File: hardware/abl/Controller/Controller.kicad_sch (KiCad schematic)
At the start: 21 parts, among them IC1 LSF0204PWJ, IC3 VEML6040A3OG, IC4 FXL6408UMX, J1 SFW20S-2STE1LF, J2 Conn_02x03_Odd_Even, J3 Conn_02x03_Odd_Even, J4 PRT-14417, J5 Conn_02x04_Odd_Even, U1 INA219AxD

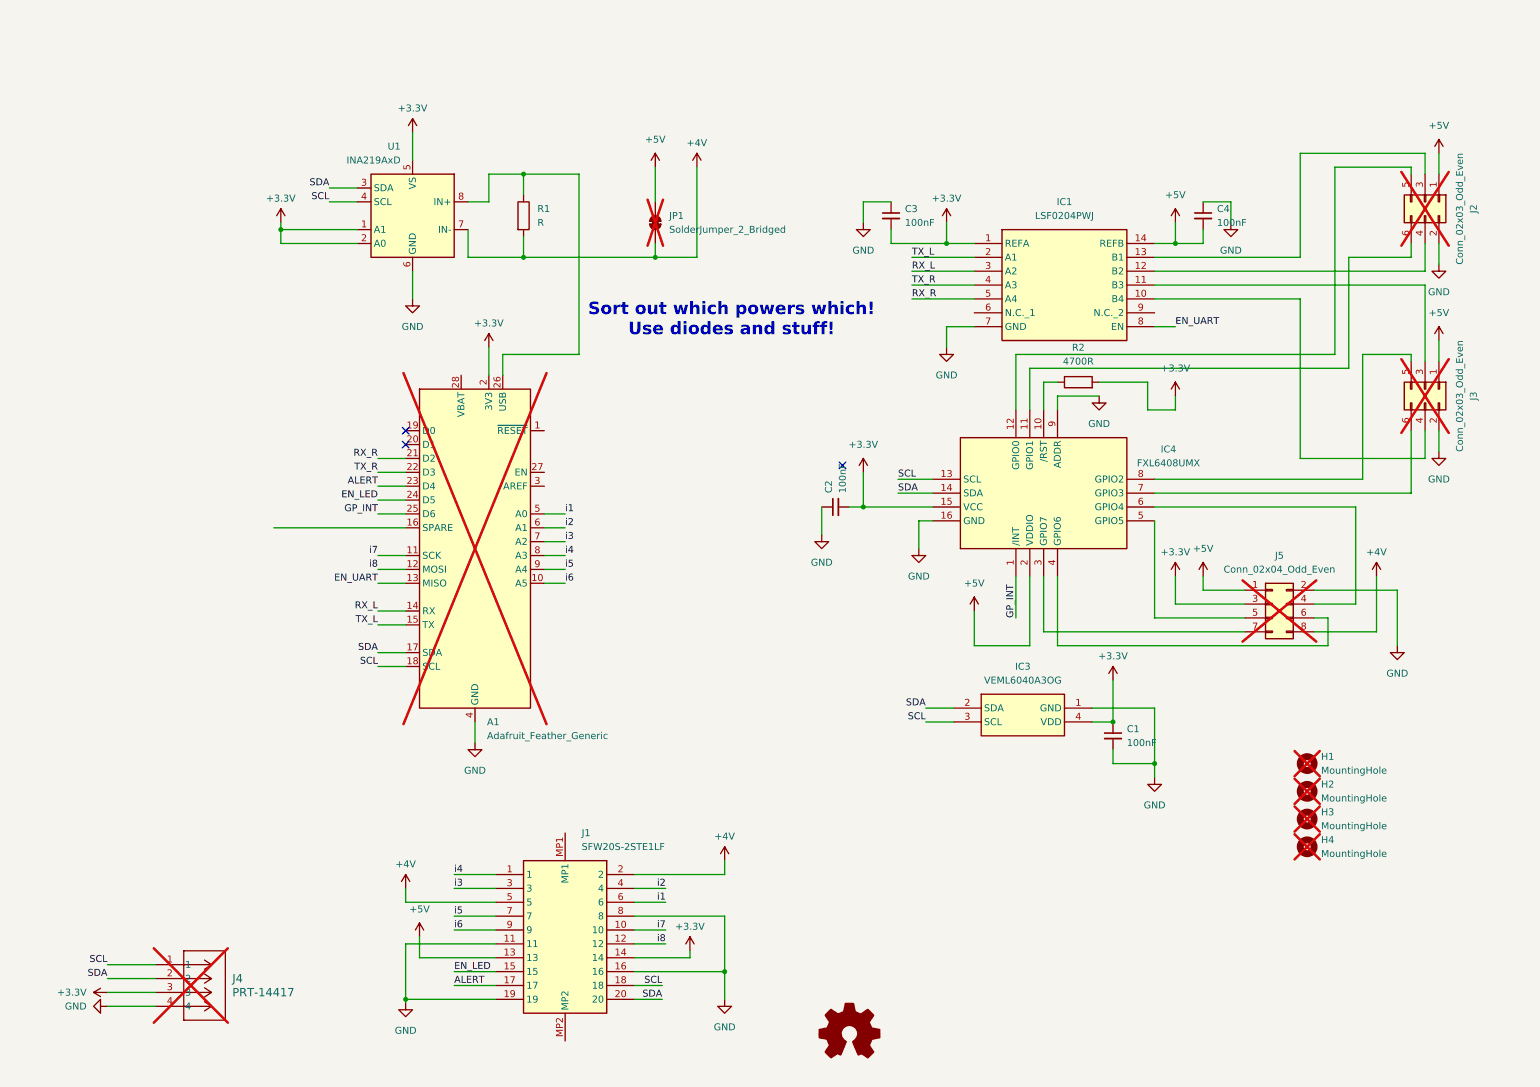
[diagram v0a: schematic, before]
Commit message: Clean up schematics and minor fixes in PCB layouts.
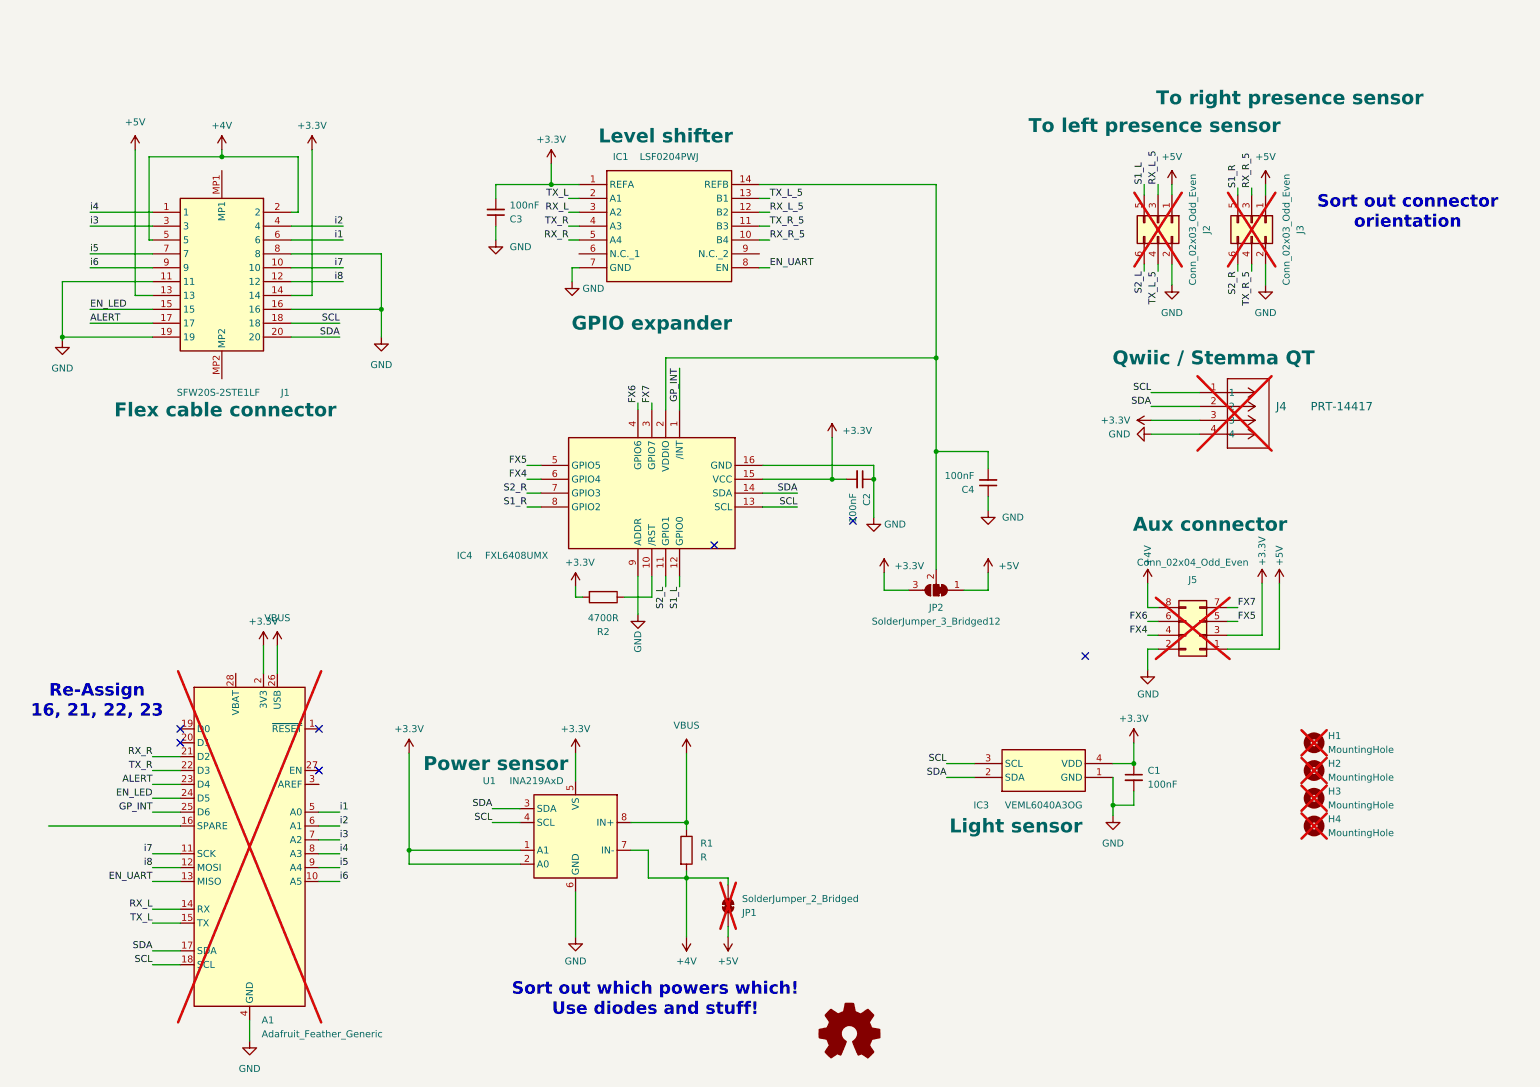
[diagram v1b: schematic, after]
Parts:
- added JP2: SolderJumper_3_Bridged12, Jumper:SolderJumper-3_P1.3mm_Bridged12_RoundedPad1.0x1.5mm, symbol Jumper:SolderJumper_3_Bridged12
- A1: Purpose (none) -> MCU
- C1, C2, C3, C4: Purpose (none) -> Decoupling
- IC1: Purpose (none) -> Level shifter
- IC3: Purpose (none) -> Light sensor
- IC4: Purpose (none) -> GPIO expander
- J1: Purpose (none) -> Flex cable connector
- J2: Purpose (none) -> To left presence sensor
- J3: Purpose (none) -> To right presence sensor
- J4: Purpose (none) -> Qwiic / Stemma QT
- J5: Purpose (none) -> Aux connector
- JP1: Purpose (none) -> Link voltages
- R1: Purpose (none) -> Current sensing
- R2: Purpose (none) -> Pull-Up
- U1: Purpose (none) -> Power sensor
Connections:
- net +3.3V: now also JP2.3 (B)
- net +5V: now also JP2.1 (A); no longer C4.2, IC1.14 (REFB), IC4.2 (VDDIO)
- net FX4: now reaches IC4.6 (GPIO4), J5.4 (Pin_4)
- net FX5: now reaches IC4.5 (GPIO5), J5.5 (Pin_5)
- net FX6: now reaches IC4.4 (GPIO6), J5.6 (Pin_6)
- net FX7: now reaches IC4.3 (GPIO7), J5.7 (Pin_7)
- net VBUS: now reaches A1.26 (USB), R1.1, U1.8 (IN+)
- net RX_R_5: now reaches J3.3 (Pin_3)
- net RX_R_5: now also IC1.10 (B4); no longer IC1.11 (B3)
- net TX_R_5: now reaches J3.4 (Pin_4)
- net TX_R_5: now also IC1.11 (B3); no longer IC1.10 (B4)
- net S1_R: now reaches IC4.8 (GPIO2), J3.5 (Pin_5)
- net S2_R: now reaches IC4.7 (GPIO3), J3.6 (Pin_6)
- net RX_L_5: now reaches J2.3 (Pin_3)
- net RX_L_5: now also IC1.12 (B2); no longer IC1.13 (B1)
- net TX_L_5: now reaches J2.4 (Pin_4)
- net TX_L_5: now also IC1.13 (B1); no longer IC1.12 (B2)
- net S1_L: now reaches IC4.12 (GPIO0), J2.5 (Pin_5)
- net S2_L: now reaches IC4.11 (GPIO1), J2.6 (Pin_6)
- new net: C4.2, IC1.14 (REFB), IC4.2 (VDDIO), JP2.2 (C)
- no-connect marks 3 -> 7
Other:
- note added: "Re-Assign 16, 21, 22, 23"
- note added: "Sort out connector orientation"
- moved on the sheet: A1, C1, C2, C3, C4, H1, H2, H3, H4, IC1, IC3, IC4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

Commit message: Improved connectors (more signals, better return paths)
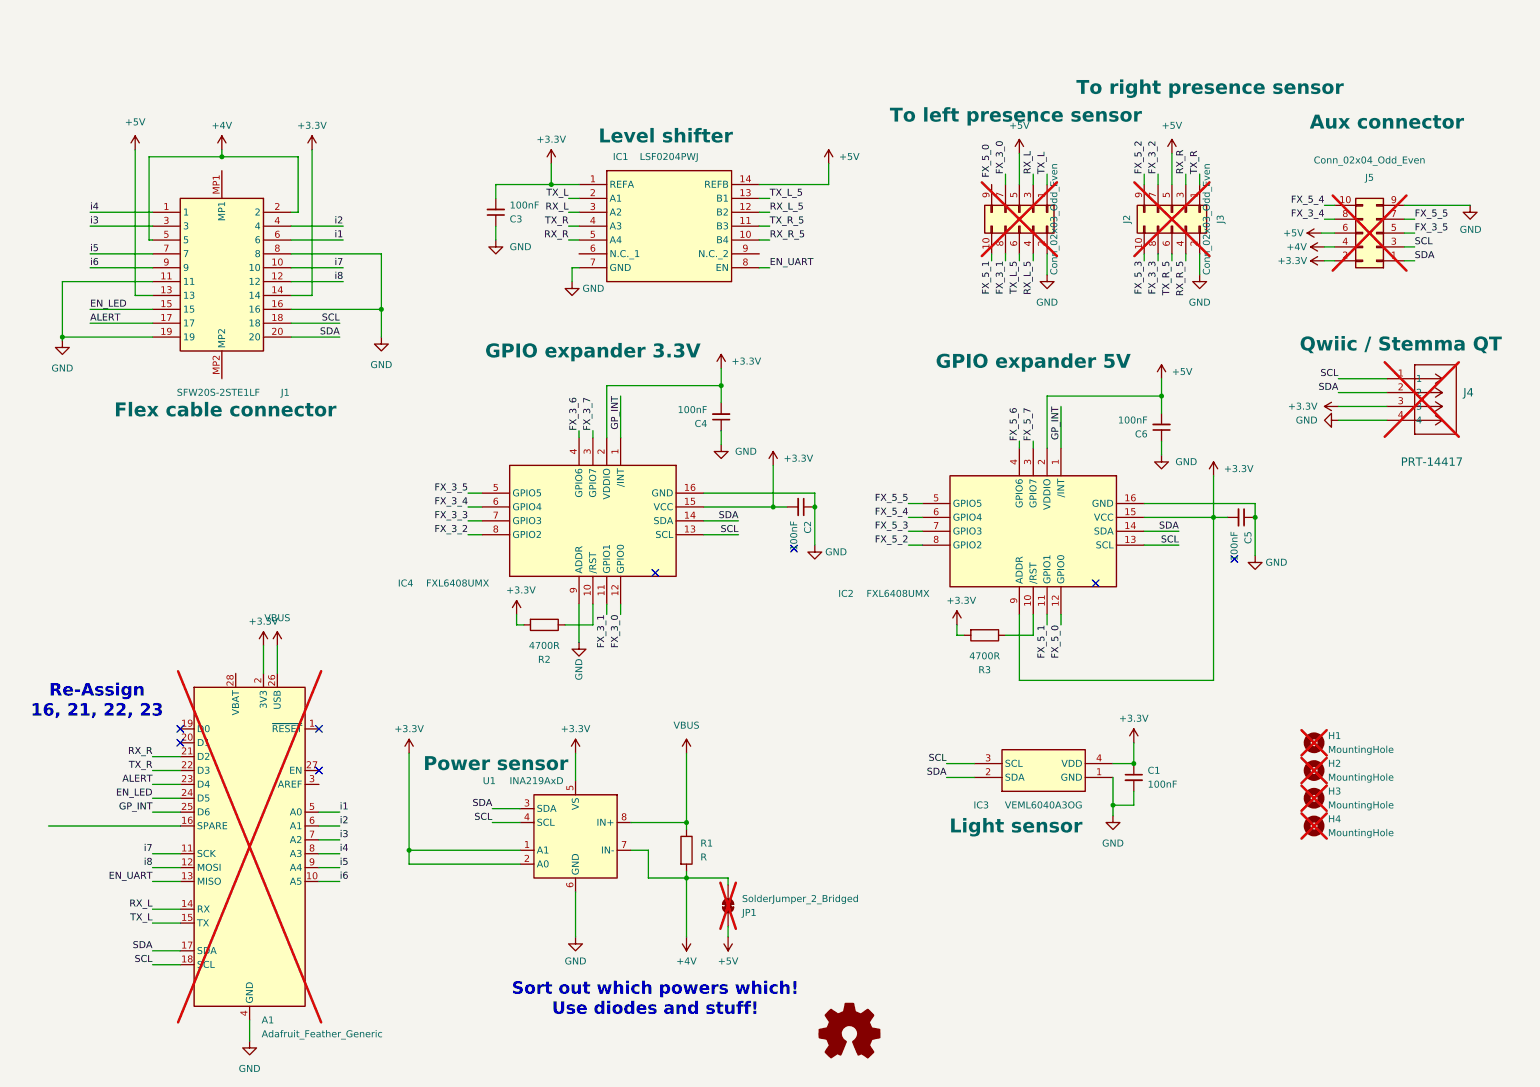
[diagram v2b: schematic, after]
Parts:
- removed JP2: SolderJumper_3_Bridged12, Jumper:SolderJumper-3_P1.3mm_Bridged12_RoundedPad1.0x1.5mm, symbol Jumper:SolderJumper_3_Bridged12
- added C5, C6: 100nF, Capacitor_SMD:C_0402_1005Metric, symbol Device:C_Small
- added IC2: FXL6408UMX, QFN40P180X260X55-16N, symbol FXL6408UMX:FXL6408UMX
- added R3: 4700R, Resistor_SMD:R_0603_1608Metric_Pad0.98x0.95mm_HandSolder, symbol Device:R
- IC4: Purpose GPIO expander -> GPIO expander 3.3V
- J2, J3: footprint Connector_IDC:IDC-Header_2x03_P2.54mm_Vertical -> Connector_IDC:IDC-Header_2x05_P2.54mm_Vertical; symbol Connector_Generic:Conn_02x03_Odd_Even -> Connector_Generic:Conn_02x05_Odd_Even
- J5: footprint Connector_IDC:IDC-Header_2x04_P2.54mm_Vertical -> Connector_IDC:IDC-Header_2x05_P2.54mm_Vertical; symbol Connector_Generic:Conn_02x04_Odd_Even -> Connector_Generic:Conn_02x05_Odd_Even
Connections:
- net +3.3V: now also C4.2, IC4.2 (VDDIO), J5.2 (Pin_2), C5.2, IC2.15 (VCC), IC2.9 (ADDR), R3.2; no longer J5.3 (Pin_3)
- net +4V: now also J5.4 (Pin_4); no longer J5.8 (Pin_8)
- net +5V: now also IC1.14 (REFB), J2.5 (Pin_5), J3.5 (Pin_5), J5.6 (Pin_6), C6.2, IC2.2 (VDDIO); no longer J2.1 (Pin_1), J3.1 (Pin_1), J5.1 (Pin_1)
- net GND: now also J5.9 (Pin_9), C5.1, C6.1, IC2.16 (GND); no longer J5.2 (Pin_2)
- net GP_INT: now also IC2.1 (/INT)
- net RX_L: now also J2.3 (Pin_3)
- net RX_L_5: now also J2.4 (Pin_4); no longer J2.3 (Pin_3)
- net RX_R: now also J3.3 (Pin_3)
- net RX_R_5: now also J3.4 (Pin_4); no longer J3.3 (Pin_3)
- net SCL: now also J5.3 (Pin_3), IC2.13 (SCL)
- net SDA: now also J5.1 (Pin_1), IC2.14 (SDA)
- net TX_L: now also J2.1 (Pin_1)
- net TX_L_5: now also J2.6 (Pin_6); no longer J2.4 (Pin_4)
- net TX_R: now also J3.1 (Pin_1)
- net TX_R_5: now also J3.6 (Pin_6); no longer J3.4 (Pin_4)
- net FX4 renamed FX_3_4
- net FX_3_4: now also J5.8 (Pin_8); no longer J5.4 (Pin_4)
- net FX5 renamed FX_3_5
- net FX6 renamed FX_3_6
- net FX_3_6: no longer J5.6 (Pin_6)
- net FX7 renamed FX_3_7
- net FX_3_7: no longer J5.7 (Pin_7)
- net S1_L renamed FX_3_0
- net FX_3_0: now also J2.7 (Pin_7); no longer J2.5 (Pin_5)
- net S1_R renamed FX_3_2
- net FX_3_2: now also J3.7 (Pin_7); no longer J3.5 (Pin_5)
- net S2_L renamed FX_3_1
- net FX_3_1: now also J2.8 (Pin_8); no longer J2.6 (Pin_6)
- net S2_R renamed FX_3_3
- net FX_3_3: now also J3.8 (Pin_8); no longer J3.6 (Pin_6)
- new net: IC2.10 (/RST), R3.1
- new net  FX_5_1: J2.10 (Pin_10)
- new net FX_5_0: IC2.12 (GPIO0)
- new net FX_5_1: IC2.11 (GPIO1)
- new net FX_5_2: IC2.8 (GPIO2), J3.9 (Pin_9)
- new net FX_5_3: IC2.7 (GPIO3), J3.10 (Pin_10)
- new net FX_5_4: IC2.6 (GPIO4), J5.10 (Pin_10)
- new net FX_5_5: IC2.5 (GPIO5), J5.7 (Pin_7)
- new net FX_5_6: IC2.4 (GPIO6)
- new net FX_5_7: IC2.3 (GPIO7)
- no-connect marks 7 -> 8
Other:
- note removed: "Sort out connector orientation"
- moved on the sheet: C2, C4, IC4, J4, R2

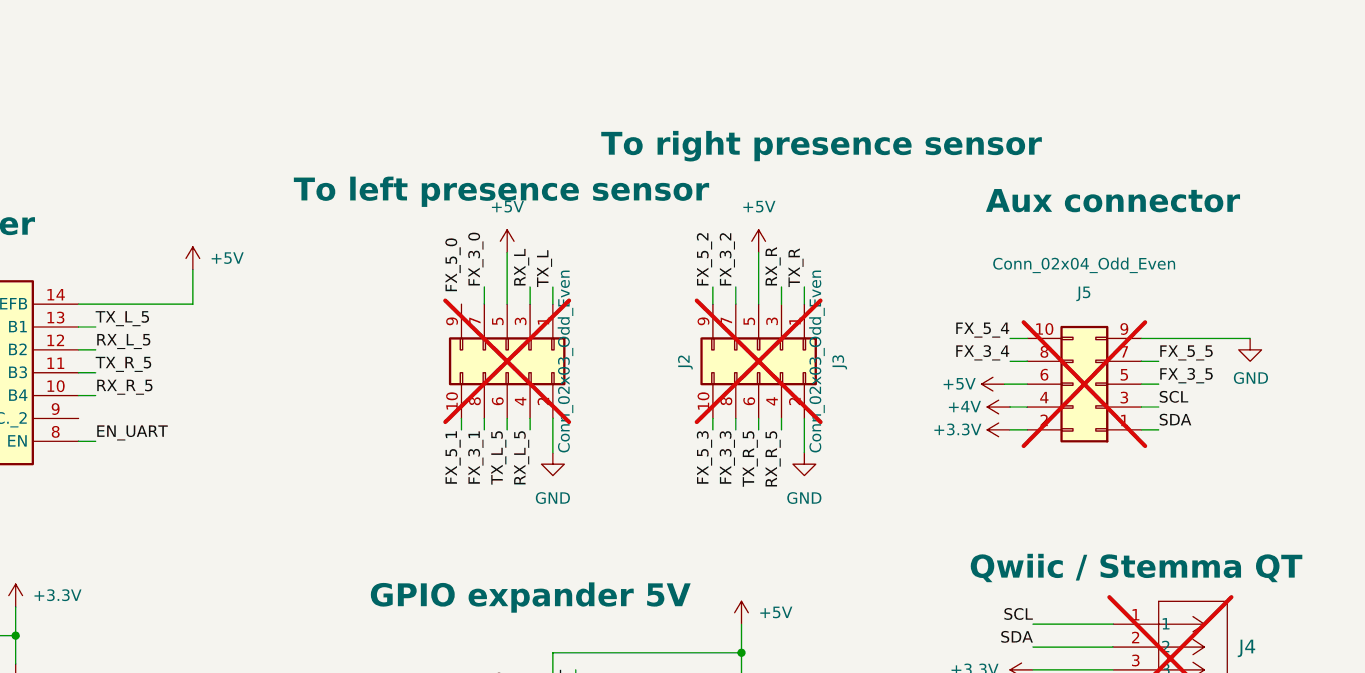
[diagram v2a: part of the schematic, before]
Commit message: Add Mosfets to power down presence sensory individually.
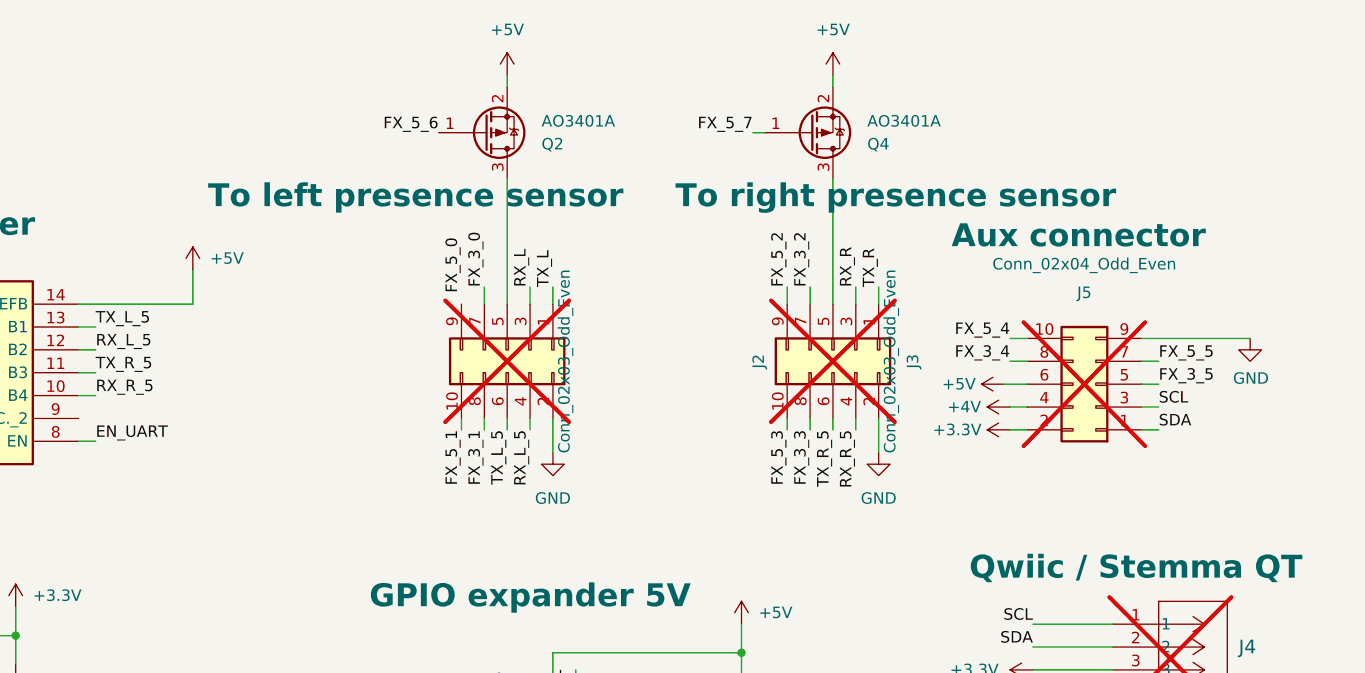
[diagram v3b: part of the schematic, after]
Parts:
- added Q2, Q4: AO3401A, Package_TO_SOT_SMD:SOT-23, symbol Transistor_FET:AO3401A
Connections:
- net +5V: now also Q2.2 (S), Q4.2 (S); no longer J2.5 (Pin_5), J3.5 (Pin_5)
- net FX_5_6: now also Q2.1 (G)
- net FX_5_7: now also Q4.1 (G)
- new net: J3.5 (Pin_5), Q4.3 (D)
- new net: J2.5 (Pin_5), Q2.3 (D)
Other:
- moved on the sheet: J3

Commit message: Metadata and minor cleanup, documentation and typo fix.
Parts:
- A1: now fitted; now left out of the parts list
- H1, H2, H3, H4, J2, J3, J4, J5, JP1: now fitted
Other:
- note added: "TODO Sort out power supply stuff:"
- note removed: "Re-Assign 16, 21, 22, 23"
- note removed: "Sort out which powers which! Use diodes and stuff!"
- title: (none) -> besteLampe! ABL Controller Module
- moved on the sheet: C1, C3, C5, C6, IC1, IC2, IC3, J1, Q2, Q4, R1, R3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

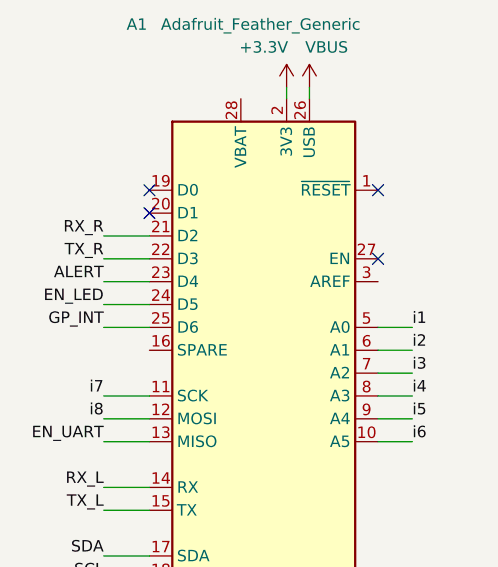
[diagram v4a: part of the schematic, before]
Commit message: Controller: Swivel GPIOs 16, 21, 22, 25 to be compatible with all three feather variants and add README.
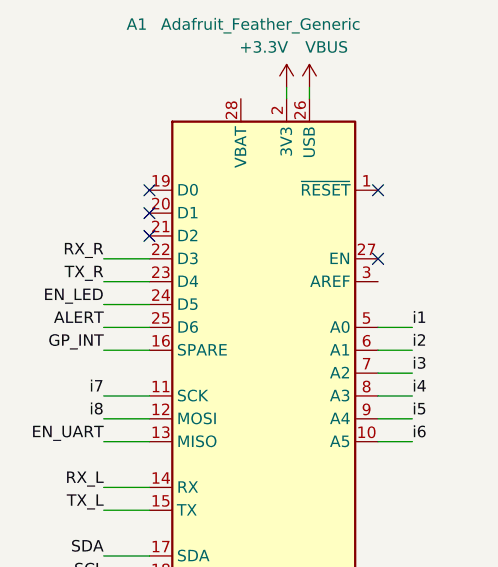
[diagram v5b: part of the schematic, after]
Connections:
- net ALERT: now also A1.25 (D6); no longer A1.23 (D4)
- net GP_INT: now also A1.16 (SPARE); no longer A1.25 (D6)
- net RX_R: now also A1.22 (D3); no longer A1.21 (D2)
- net TX_R: now also A1.23 (D4); no longer A1.22 (D3)
- no-connect marks 8 -> 9
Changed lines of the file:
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@@
+	)
+	(no_connect
+		(at 28.575 140.335)
 	)
 	(no_connect
@@
 	(wire
 		(pts
+			(xy 23.495 153.035) (xy 28.575 153.035)
+		)
+		(stroke
+			(width 0)
+			(type default)
+		)
+	)
+	(wire
+		(pts
 			(xy 236.855 121.92) (xy 224.155 121.92)
 		)
@@
 		(pts
 			(xy 34.925 33.655) (xy 34.925 60.325)
-		)
-		(stroke
-			(width 0)
-			(type default)
-		)
-	)
-	(wire
-		(pts
-			(xy 23.495 140.335) (xy 28.575 140.335)
 		)
 		(stroke
@@
 	)
 	(label "TX_R"
-		(at 23.495 142.875 180)
+		(at 23.495 145.415 180)
 		(fields_autoplaced yes)
 		(effects
@@
 	)
 	(label "RX_R"
-		(at 23.495 140.335 180)
+		(at 23.495 142.875 180)
 		(fields_autoplaced yes)
 		(effects
@@
 	)
 	(label "ALERT"
-		(at 23.495 145.415 180)
+		(at 23.495 150.495 180)
 		(fields_autoplaced yes)
 		(effects
@@
 	)
 	(label "GP_INT"
-		(at 23.495 150.495 180)
-		(fields_autoplaced yes)
-		(effects
+		(at 23.495 153.035 180)
+		(fields_autoplaced yes)
+		(effects
